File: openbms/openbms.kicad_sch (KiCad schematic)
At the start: 0 parts

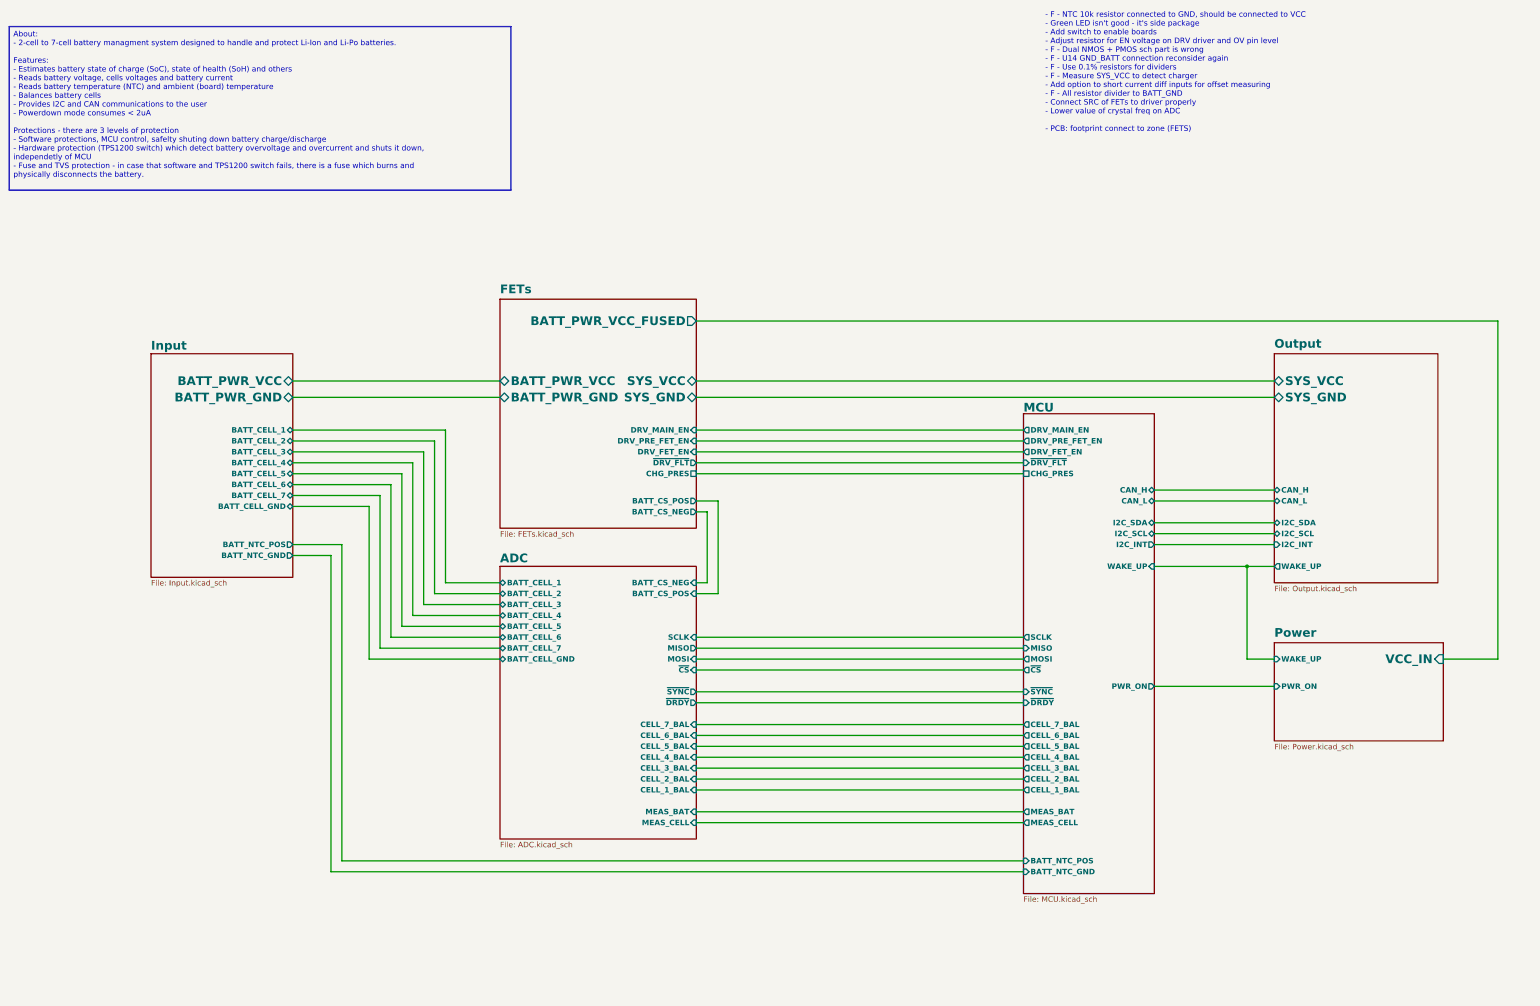
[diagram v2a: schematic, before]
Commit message: Option to shortcut current ADC sensor added
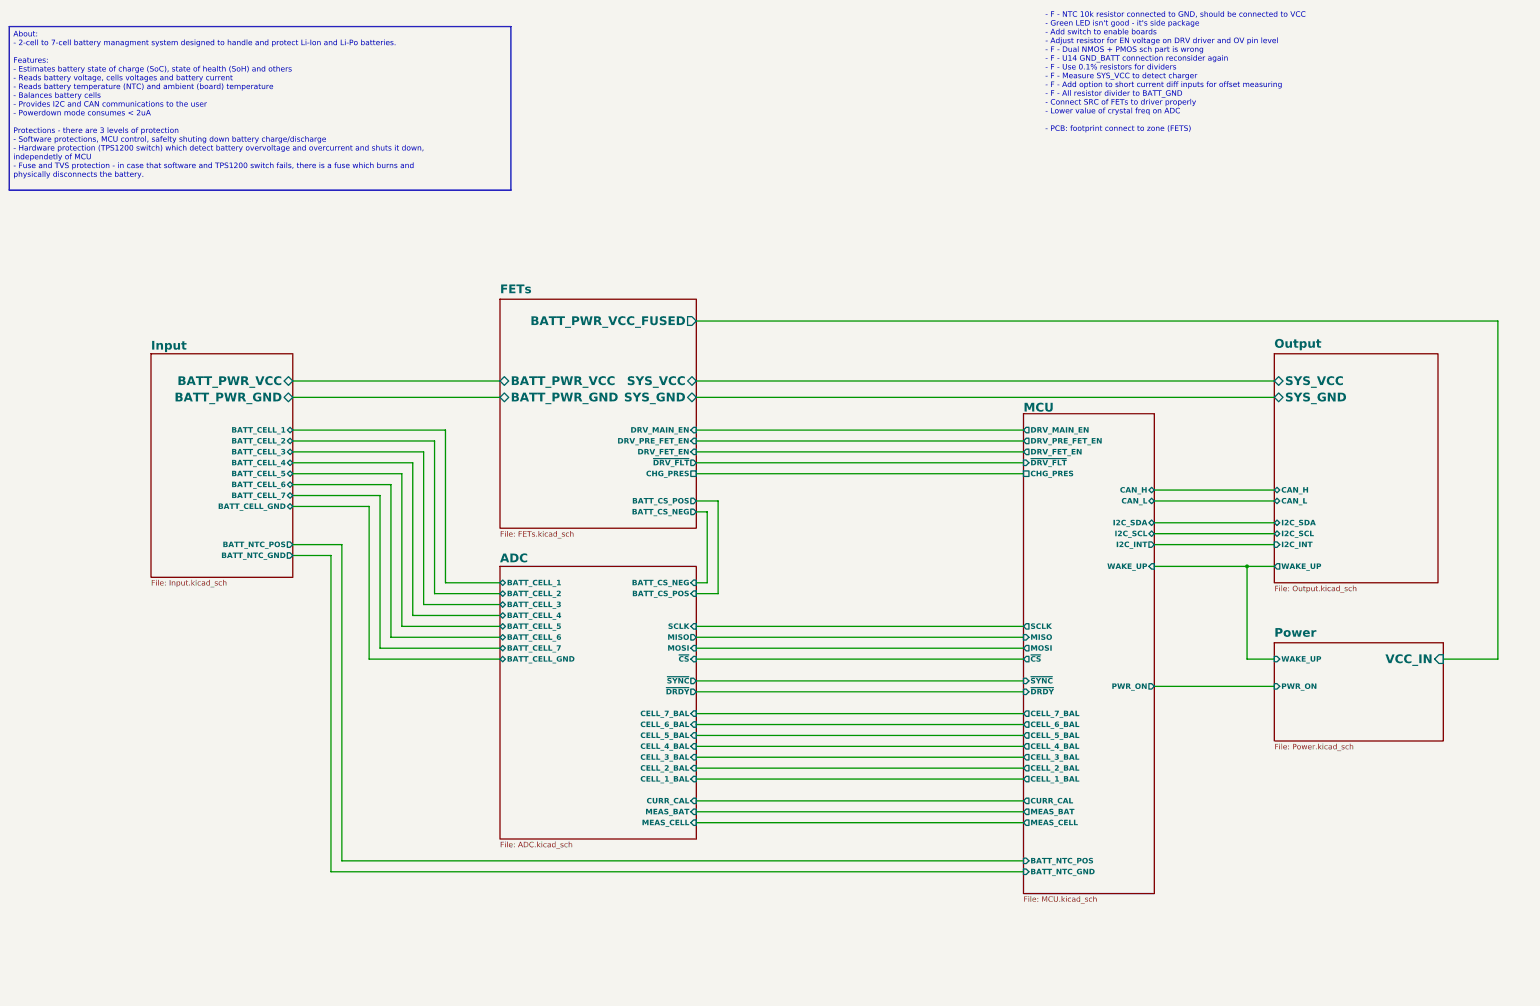
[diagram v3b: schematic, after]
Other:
- sheet ADC ports: added CURR_CAL; removed none
- sheet MCU ports: added CURR_CAL; removed none
- note added: "- F - NTC 10k resistor connected to GND, should be connected to VCC - Green LED isn't good - it's side package - Add switch to enable boards - Adjust resistor for EN voltage on DRV driver and OV pin level - F - Dual NMOS + PMOS sch part is wrong - F - U14 GND_BATT connection reconsider again - F - Use 0.1% resistors for dividers - F - Measure SYS_VCC to detect charger - F - Add option to short cu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"
- note removed: "- F - NTC 10k resistor connected to GND, should be connected to VCC - Green LED isn't good - it's side package - Add switch to enable boards - Adjust resistor for EN voltage on DRV driver and OV pin level - F - Dual NMOS + PMOS sch part is wrong - F - U14 GND_BATT connection reconsider again - F - Use 0.1% resistors for dividers - F - Measure SYS_VCC to detect charger - Add option to short curren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"

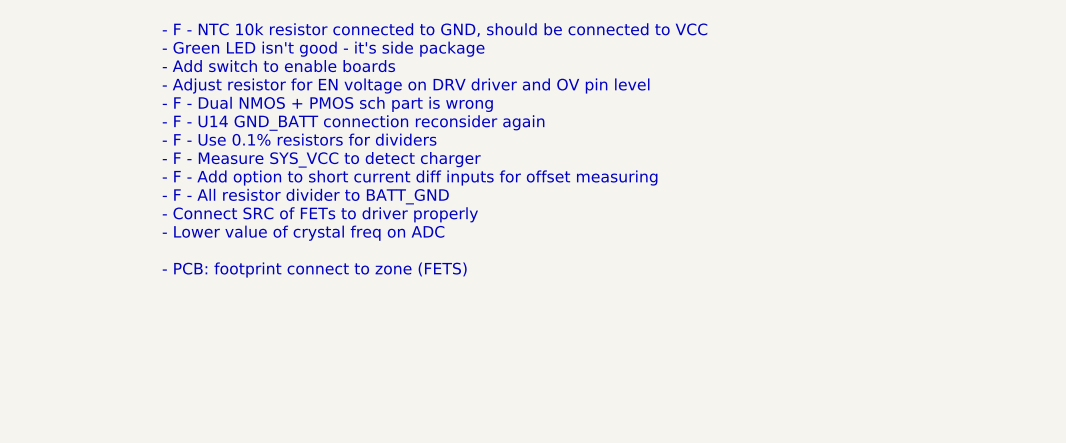
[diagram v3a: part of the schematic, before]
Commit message: Button for quick enable added
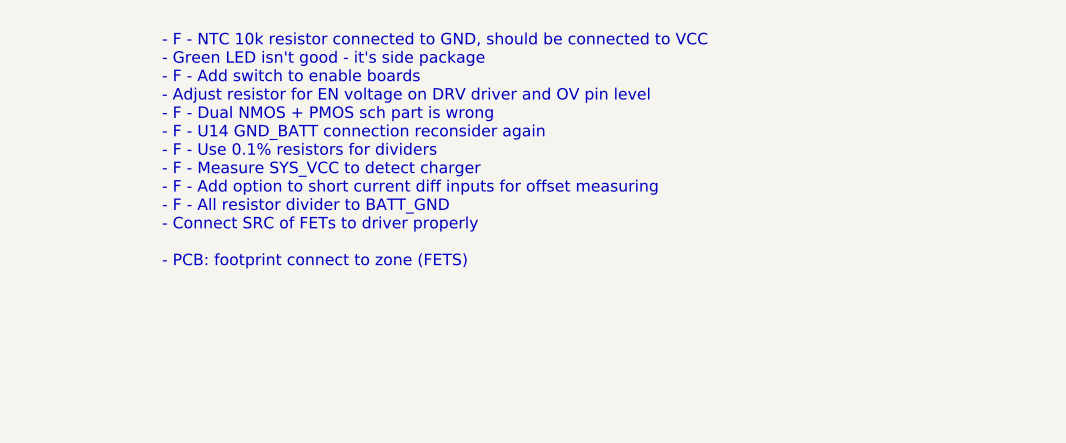
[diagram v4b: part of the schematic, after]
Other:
- note added: "- F - NTC 10k resistor connected to GND, should be connected to VCC - Green LED isn't good - it's side package - F - Add switch to enable boards - Adjust resistor for EN voltage on DRV driver and OV pin level - F - Dual NMOS + PMOS sch part is wrong - F - U14 GND_BATT connection reconsider again - F - Use 0.1% resistors for dividers - F - Measure SYS_VCC to detect charger - F - Add option to shor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"
- note removed: "- F - NTC 10k resistor connected to GND, should be connected to VCC - Green LED isn't good - it's side package - Add switch to enable boards - Adjust resistor for EN voltage on DRV driver and OV pin level - F - Dual NMOS + PMOS sch part is wrong - F - U14 GND_BATT connection reconsider again - F - Use 0.1% resistors for dividers - F - Measure SYS_VCC to detect charger - F - Add option to short cu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"
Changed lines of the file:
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@@
 		(comment 4 "Open Source Battery Management System")
 	)
-	(text "- F - NTC 10k resistor connected to GND, should be connected to VCC\n- Green LED isn't good - it's side package\n- Add switch to enable boards\n- Adjust resistor for EN voltage on DRV driver and OV pin level\n- F - Dual NMOS + PMOS sch part is wrong\n- F - U14 GND_BATT connection reconsider again\n- F - Use 0.1% resistors for dividers\n- F - Measure SYS_VCC to detect charger\n- F - Add option to short current diff inputs for offset measuring\n- F - All resistor divider to BATT_GND\n- Connect SRC of FETs to driver properly\n- Lower value of crystal freq on ADC\n\n- PCB: footprint connect to zone (FETS)\n"
+	(text "- F - NTC 10k resistor connected to GND, should be connected to VCC\n- Green LED isn't good - it's side package\n- F - Add switch to enable boards\n- Adjust resistor for EN voltage on DRV driver and OV pin level\n- F - Dual NMOS + PMOS sch part is wrong\n- F - U14 GND_BATT connection reconsider again\n- F - Use 0.1% resistors for dividers\n- F - Measure SYS_VCC to detect charger\n- F - Add option to short current diff inputs for offset measuring\n- F - All resistor divider to BATT_GND\n- Connect SRC of FETs to driver properly\n\n- PCB: footprint connect to zone (FETS)\n"
 		(exclude_from_sim no)
 		(at 259.08 28.448 0)

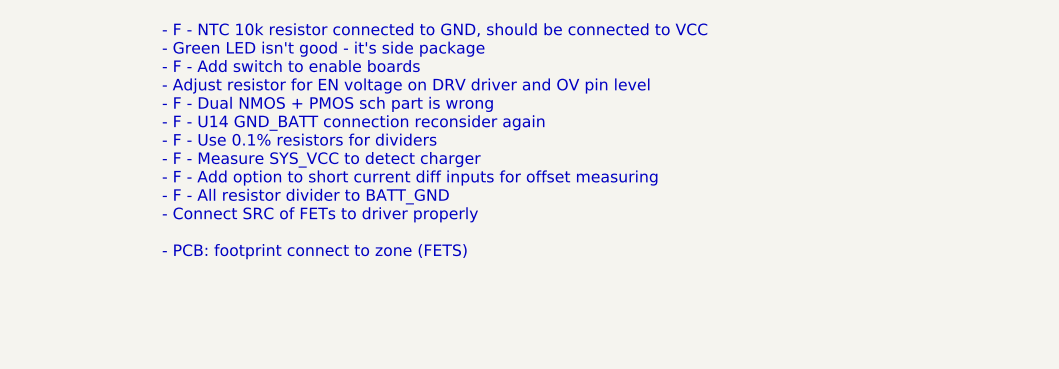
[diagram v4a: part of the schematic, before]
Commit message: FET driver EN and OV pin voltage levels fixed
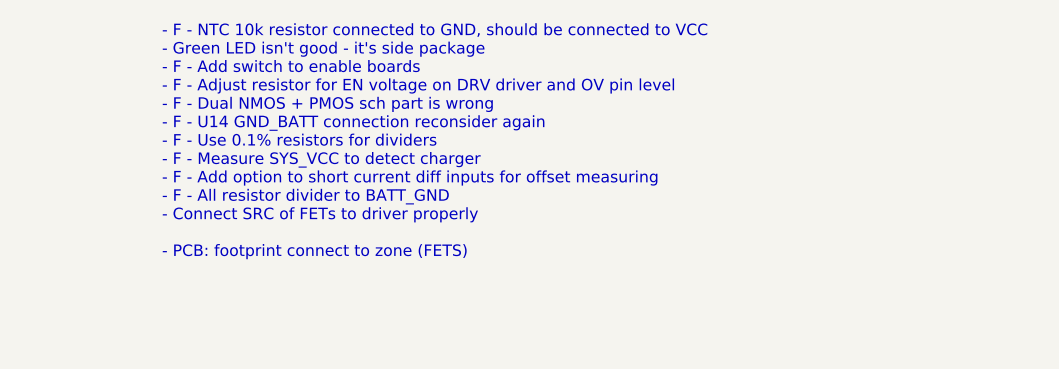
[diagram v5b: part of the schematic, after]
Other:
- note added: "- F - NTC 10k resistor connected to GND, should be connected to VCC - Green LED isn't good - it's side package - F - Add switch to enable boards - F - Adjust resistor for EN voltage on DRV driver and OV pin level - F - Dual NMOS + PMOS sch part is wrong - F - U14 GND_BATT connection reconsider again - F - Use 0.1% resistors for dividers - F - Measure SYS_VCC to detect charger - F - Add option to 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"
- note removed: "- F - NTC 10k resistor connected to GND, should be connected to VCC - Green LED isn't good - it's side package - F - Add switch to enable boards - Adjust resistor for EN voltage on DRV driver and OV pin level - F - Dual NMOS + PMOS sch part is wrong - F - U14 GND_BATT connection reconsider again - F - Use 0.1% resistors for dividers - F - Measure SYS_VCC to detect charger - F - Add option to shor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"
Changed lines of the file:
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@@
 		(comment 4 "Open Source Battery Management System")
 	)
-	(text "- F - NTC 10k resistor connected to GND, should be connected to VCC\n- Green LED isn't good - it's side package\n- F - Add switch to enable boards\n- Adjust resistor for EN voltage on DRV driver and OV pin level\n- F - Dual NMOS + PMOS sch part is wrong\n- F - U14 GND_BATT connection reconsider again\n- F - Use 0.1% resistors for dividers\n- F - Measure SYS_VCC to detect charger\n- F - Add option to short current diff inputs for offset measuring\n- F - All resistor divider to BATT_GND\n- Connect SRC of FETs to driver properly\n\n- PCB: footprint connect to zone (FETS)\n"
+	(text "- F - NTC 10k resistor connected to GND, should be connected to VCC\n- Green LED isn't good - it's side package\n- F - Add switch to enable boards\n- F - Adjust resistor for EN voltage on DRV driver and OV pin level\n- F - Dual NMOS + PMOS sch part is wrong\n- F - U14 GND_BATT connection reconsider again\n- F - Use 0.1% resistors for dividers\n- F - Measure SYS_VCC to detect charger\n- F - Add option to short current diff inputs for offset measuring\n- F - All resistor divider to BATT_GND\n- Connect SRC of FETs to driver properly\n\n- PCB: footprint connect to zone (FETS)\n"
 		(exclude_from_sim no)
 		(at 259.08 28.448 0)

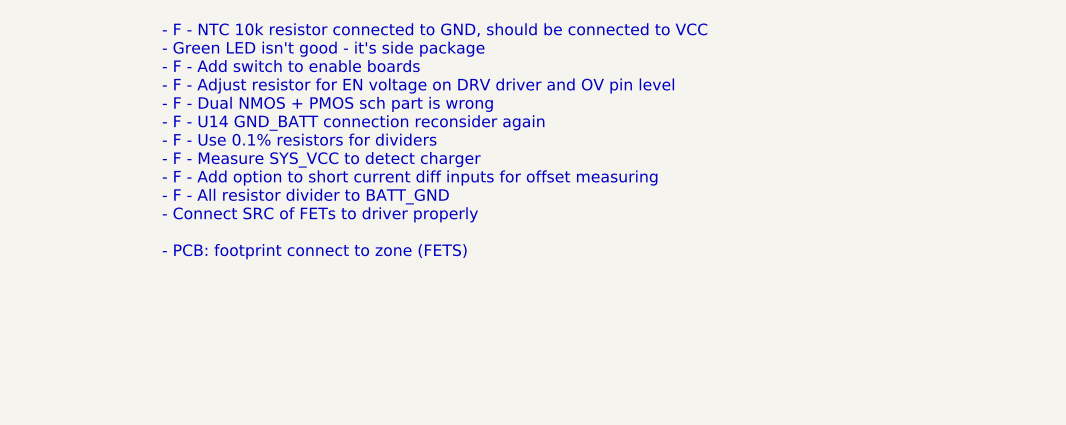
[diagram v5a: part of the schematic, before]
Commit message: Polygon zone fixed, SRC net in FET fixed
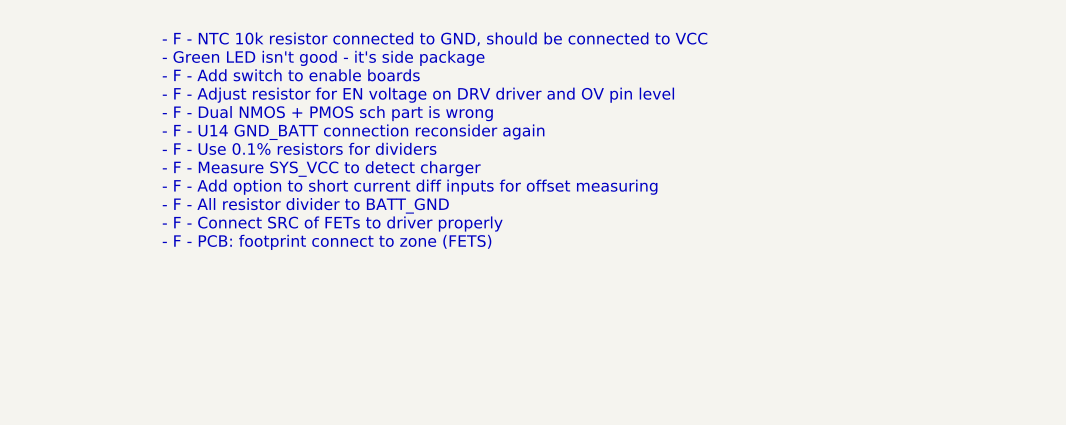
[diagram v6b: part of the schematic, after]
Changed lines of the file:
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@@
 		(comment 4 "Open Source Battery Management System")
 	)
-	(text "- F - NTC 10k resistor connected to GND, should be connected to VCC\n- Green LED isn't good - it's side package\n- F - Add switch to enable boards\n- F - Adjust resistor for EN voltage on DRV driver and OV pin level\n- F - Dual NMOS + PMOS sch part is wrong\n- F - U14 GND_BATT connection reconsider again\n- F - Use 0.1% resistors for dividers\n- F - Measure SYS_VCC to detect charger\n- F - Add option to short current diff inputs for offset measuring\n- F - All resistor divider to BATT_GND\n- Connect SRC of FETs to driver properly\n\n- PCB: footprint connect to zone (FETS)\n"
+	(text "- F - NTC 10k resistor connected to GND, should be connected to VCC\n- Green LED isn't good - it's side package\n- F - Add switch to enable boards\n- F - Adjust resistor for EN voltage on DRV driver and OV pin level\n- F - Dual NMOS + PMOS sch part is wrong\n- F - U14 GND_BATT connection reconsider again\n- F - Use 0.1% resistors for dividers\n- F - Measure SYS_VCC to detect charger\n- F - Add option to short current diff inputs for offset measuring\n- F - All resistor divider to BATT_GND\n- F - Connect SRC of FETs to driver properly\n- F - PCB: footprint connect to zone (FETS)\n"
 		(exclude_from_sim no)
 		(at 259.08 28.448 0)
